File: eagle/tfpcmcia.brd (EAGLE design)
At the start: 80.4 x 44.4 mm, 36 parts, among them IC1 CH32V307, IC2 LM1117MPX-3.3, IC3 APS6404L-3SQR-SN, IC4 MCP6001RT-I_OT, J2 MSD-11-A

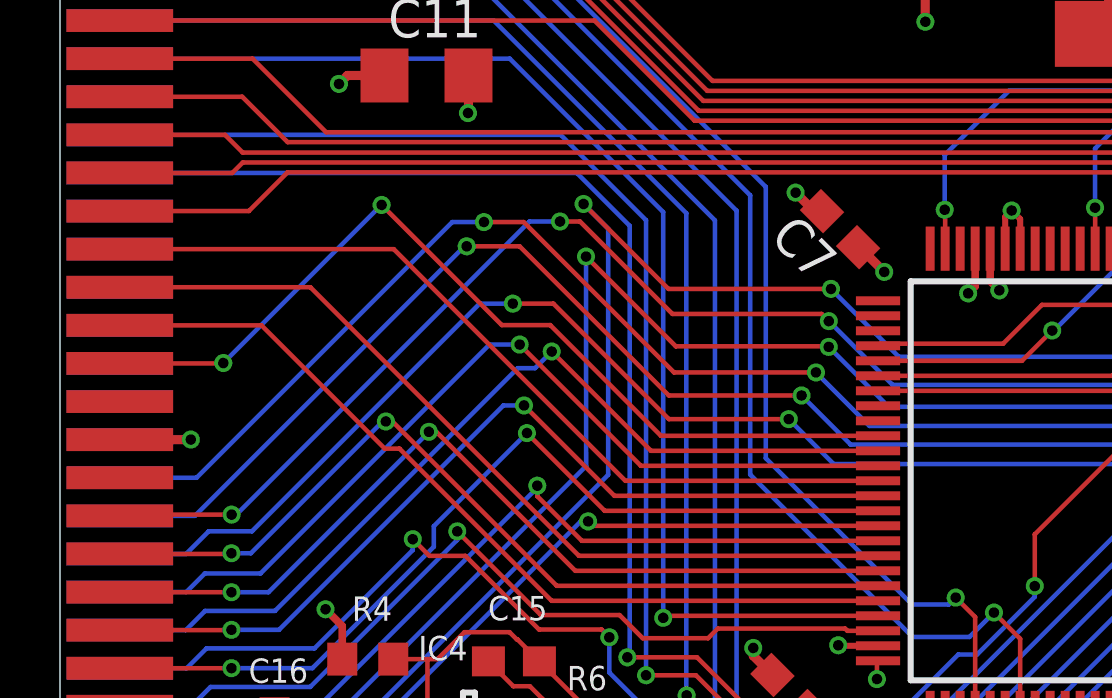
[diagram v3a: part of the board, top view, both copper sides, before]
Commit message: Updated READY signal and updated pinout specs
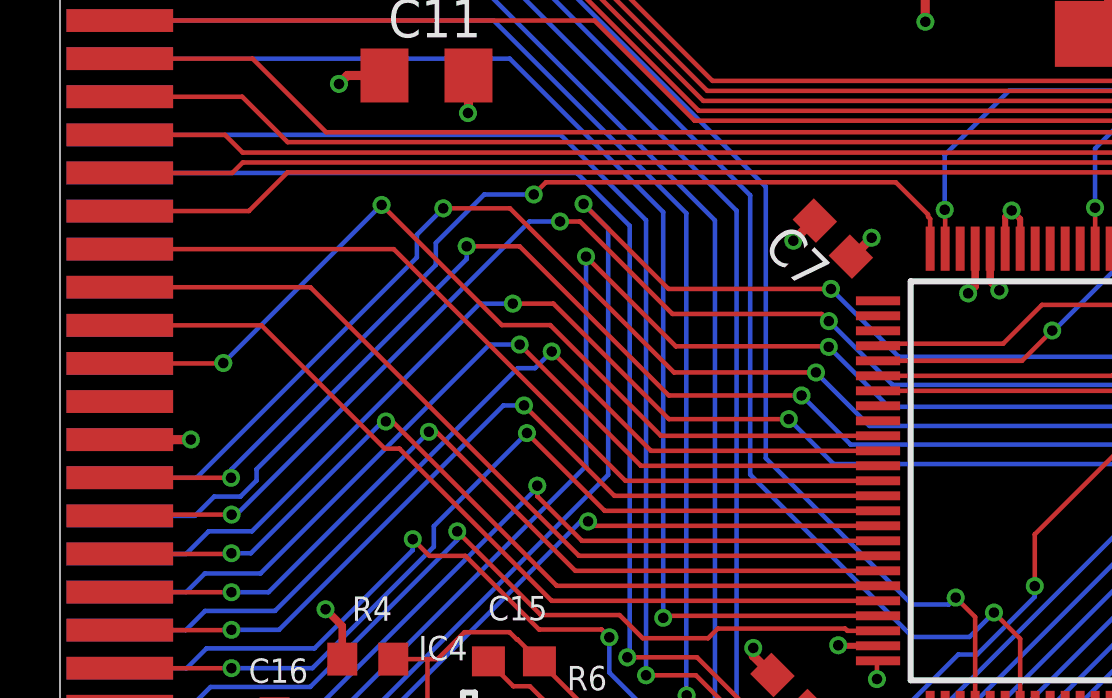
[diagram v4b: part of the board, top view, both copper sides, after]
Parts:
- moved C7 0.40 mm to (25.8, 28.2)
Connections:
- net READY: now also IC1.25
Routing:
- net READY: track 0.00 -> 33.2 mm, vias 0 -> 2
- net A21: track 47.2 -> 48.1 mm
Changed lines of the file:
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@@
 <attribute name="VALUE" x="42.162915625" y="28.52758125" size="1.27" layer="27" rot="R315"/>
 </element>
-<element name="C7" library="eagle-ltspice" library_urn="urn:adsk.eagle:library:217" package="C0603" package3d_urn="urn:adsk.eagle:package:13262/1" value="100nF" x="26.00196875" y="28.468321875" smashed="yes" rot="R135">
-<attribute name="NAME" x="26.00196875" y="27.57029375" size="1.27" layer="25" rot="R135"/>
-<attribute name="SPICEMODEL" value="NONE" x="26.00196875" y="28.468321875" size="0.8128" layer="27" rot="R135" display="off"/>
-<attribute name="SPICEPREFIX" value="C" x="26.00196875" y="28.468321875" size="0.8128" layer="27" rot="R135" display="off"/>
-<attribute name="VALUE" x="27.79801875" y="29.366346875" size="1.27" layer="27" rot="R135"/>
+<element name="C7" library="eagle-ltspice" library_urn="urn:adsk.eagle:library:217" package="C0603" package3d_urn="urn:adsk.eagle:package:13262/1" value="100nF" x="25.7622" y="28.153596875" smashed="yes" rot="R135">
+<attribute name="NAME" x="25.7622" y="27.25556875" size="1.27" layer="25" rot="R135"/>
+<attribute name="SPICEMODEL" value="NONE" x="25.7622" y="28.153596875" size="0.8128" layer="27" rot="R135" display="off"/>
+<attribute name="SPICEPREFIX" value="C" x="25.7622" y="28.153596875" size="0.8128" layer="27" rot="R135" display="off"/>
+<attribute name="VALUE" x="27.55825" y="29.051621875" size="1.27" layer="27" rot="R135"/>
 </element>
 <element name="C8" library="eagle-ltspice" library_urn="urn:adsk.eagle:library:217" package="C0603" package3d_urn="urn:adsk.eagle:package:13262/1" value="100nF" x="43.799840625" y="10.20089375" smashed="yes">
@@
 <contactref element="C9" pad="2"/>
 <via x="51.974821875" y="29.75490625" extent="1-16" drill="0.35"/>
-<via x="24.519659375" y="29.68626875" extent="1-16" drill="0.35"/>
+<via x="24.44473125" y="28.082671875" extent="1-16" drill="0.35"/>
 <via x="45.67343125" y="10.182284375" extent="1-16" drill="0.35"/>
 <via x="23.108325" y="14.508578125" extent="1-16" drill="0.35"/>
@@
 <wire x1="13.615446875" y1="32.354225" x2="13.599446875" y2="32.338225" width="0.3048" layer="1"/>
 <via x="13.599446875" y="32.338225" extent="1-16" drill="0.35"/>
-<wire x1="25.400925" y1="29.0693625" x2="25.136565625" y2="29.0693625" width="0.3048" layer="1"/>
-<wire x1="25.136565625" y1="29.0693625" x2="24.519659375" y2="29.68626875" width="0.3048" layer="1"/>
+<wire x1="25.16115625" y1="28.7546375" x2="25.116696875" y2="28.7546375" width="0.3048" layer="1"/>
+<wire x1="25.116696875" y1="28.7546375" x2="24.44473125" y2="28.082671875" width="0.3048" layer="1"/>
 <wire x1="48.549784375" y1="22.454765625" x2="48.61005625" y2="22.39449375" width="0.3048" layer="1"/>
 <wire x1="48.61005625" y1="22.39449375" x2="48.61005625" y2="21.304909375" width="0.3048" layer="1"/>
@@
 <signal name="READY">
 <contactref element="PCMCIA" pad="16"/>
+<wire x1="1.991615625" y1="20.18208125" x2="5.6981875" y2="20.18208125" width="0.1524" layer="1"/>
+<wire x1="5.6981875" y1="20.18208125" x2="5.701259375" y2="20.179009375" width="0.1524" layer="1"/>
+<via x="5.701259375" y="20.179009375" extent="1-16" drill="0.35"/>
+<wire x1="5.701259375" y1="20.179009375" x2="5.701259375" y2="20.44955" width="0.1524" layer="16"/>
+<wire x1="12.527703125" y1="27.27599375" x2="5.701259375" y2="20.44955" width="0.1524" layer="16"/>
+<wire x1="12.527703125" y1="27.27599375" x2="12.527703125" y2="28.010809375" width="0.1524" layer="16"/>
+<via x="15.79174375" y="29.624234375" extent="1-16" drill="0.35"/>
+<wire x1="15.79174375" y1="29.624234375" x2="16.198278125" y2="30.03076875" width="0.1524" layer="1"/>
+<contactref element="IC1" pad="25"/>
+<wire x1="28.9347875" y1="28.956984375" x2="28.9347875" y2="28.88495" width="0.1524" layer="1"/>
+<wire x1="28.9347875" y1="28.88495" x2="29.005509375" y2="28.814228125" width="0.1524" layer="1"/>
+<wire x1="29.005509375" y1="28.814228125" x2="29.005509375" y2="27.81800625" width="0.1524" layer="1"/>
+<wire x1="16.198278125" y1="30.03076875" x2="27.861003125" y2="30.03076875" width="0.1524" layer="1"/>
+<wire x1="27.861003125" y1="30.03076875" x2="28.9347875" y2="28.956984375" width="0.1524" layer="1"/>
+<wire x1="12.527703125" y1="28.010809375" x2="14.141128125" y2="29.624234375" width="0.1524" layer="16"/>
+<wire x1="14.141128125" y1="29.624234375" x2="15.79174375" y2="29.624234375" width="0.1524" layer="16"/>
 </signal>
 <signal name="VCC">
@@
 <contactref element="PCMCIA" pad="49"/>
 <contactref element="IC1" pad="90"/>
-<wire x1="13.48235" y1="27.897071875" x2="13.556803125" y2="27.897071875" width="0.1524" layer="16"/>
 <wire x1="42.743509375" y1="21.08000625" x2="37.259575" y2="21.08000625" width="0.1524" layer="1"/>
 <wire x1="37.259575" y1="21.08000625" x2="37.051959375" y2="21.287621875" width="0.1524" layer="1"/>
@@
 <wire x1="20.29363125" y1="22.9238875" x2="15.320446875" y2="27.897071875" width="0.1524" layer="1"/>
 <wire x1="1.991615625" y1="18.91208125" x2="4.497359375" y2="18.91208125" width="0.1524" layer="16"/>
-<wire x1="4.497359375" y1="18.91208125" x2="13.48235" y2="27.897071875" width="0.1524" layer="16"/>
+<wire x1="4.497359375" y1="18.91208125" x2="5.139271875" y2="19.55399375" width="0.1524" layer="16"/>
+<wire x1="13.556803125" y1="27.472684375" x2="13.556803125" y2="27.897071875" width="0.1524" layer="16"/>
+<wire x1="6.55244375" y1="20.468325" x2="13.556803125" y2="27.472684375" width="0.1524" layer="16"/>
+<wire x1="6.55244375" y1="20.09373125" x2="6.55244375" y2="20.468325" width="0.1524" layer="16"/>
+<wire x1="5.139271875" y1="19.55399375" x2="6.01270625" y2="19.55399375" width="0.1524" layer="16"/>
+<wire x1="6.01270625" y1="19.55399375" x2="6.55244375" y2="20.09373125" width="0.1524" layer="16"/>
 </signal>
 <signal name="A21">
@@
 <contactref element="IC1" pad="91"/>
 <wire x1="1.991615625" y1="20.18208125" x2="4.552246875" y2="20.18208125" width="0.1524" layer="16"/>
-<wire x1="13.075053125" y1="28.7048875" x2="4.552246875" y2="20.18208125" width="0.1524" layer="16"/>
-<wire x1="13.075053125" y1="28.7048875" x2="14.131571875" y2="28.7048875" width="0.1524" layer="16"/>
+<wire x1="11.8960125" y1="27.525846875" x2="4.552246875" y2="20.18208125" width="0.1524" layer="16"/>
 <wire x1="42.743509375" y1="21.58000625" x2="38.032721875" y2="21.58000625" width="0.1524" layer="1"/>
 <wire x1="38.032721875" y1="21.58000625" x2="37.7038625" y2="21.908865625" width="0.1524" layer="1"/>
@@
 <via x="25.19799375" y="23.692453125" extent="1-16" drill="0.35"/>
 <wire x1="25.19799375" y1="23.692453125" x2="20.468790625" y2="23.692453125" width="0.1524" layer="1"/>
-<wire x1="15.45635625" y1="28.7048875" x2="14.131571875" y2="28.7048875" width="0.1524" layer="1"/>
-<via x="14.131571875" y="28.7048875" extent="1-16" drill="0.35"/>
-<wire x1="20.468790625" y1="23.692453125" x2="15.45635625" y2="28.7048875" width="0.1524" layer="1"/>
+<wire x1="14.9992" y1="29.16204375" x2="12.775275" y2="29.16204375" width="0.1524" layer="1"/>
+<via x="12.775275" y="29.16204375" extent="1-16" drill="0.35"/>
+<wire x1="20.468790625" y1="23.692453125" x2="14.9992" y2="29.16204375" width="0.1524" layer="1"/>
+<wire x1="12.775275" y1="29.16204375" x2="11.8960125" y2="28.28278125" width="0.1524" layer="16"/>
+<wire x1="11.8960125" y1="28.28278125" x2="11.8960125" y2="27.525846875" width="0.1524" layer="16"/>
 </signal>
 <signal name="A22">
@@
 <contactref element="C9" pad="1"/>
 <via x="52.0015875" y="33.392221875" extent="1-16" drill="0.35"/>
-<via x="27.47450625" y="27.043275" extent="1-16" drill="0.35"/>
+<via x="27.0549125" y="28.182278125" extent="1-16" drill="0.35"/>
 <wire x1="41.880825" y1="10.20089375" x2="41.8673125" y2="10.21440625" width="0.1524" layer="1"/>
 <via x="41.8673125" y="10.21440625" extent="1-16" drill="0.35"/>
@@
 <via x="42.61121875" y="30.702096875" extent="1-16" drill="0.35"/>
 <via x="45.696228125" y="22.461528125" extent="1-16" drill="0.35"/>
-<wire x1="26.603009375" y1="27.867278125" x2="26.650503125" y2="27.867278125" width="0.3048" layer="1"/>
-<wire x1="26.650503125" y1="27.867278125" x2="27.47450625" y2="27.043275" width="0.3048" layer="1"/>
+<wire x1="26.363240625" y1="27.552553125" x2="26.4251875" y2="27.552553125" width="0.3048" layer="1"/>
+<wire x1="26.4251875" y1="27.552553125" x2="27.0549125" y2="28.182278125" width="0.3048" layer="1"/>
 <wire x1="45.696228125" y1="22.461528125" x2="46.843021875" y2="22.461528125" width="0.3048" layer="1"/>
 <wire x1="46.843021875" y1="22.461528125" x2="46.849784375" y2="22.454765625" width="0.3048" layer="1"/>

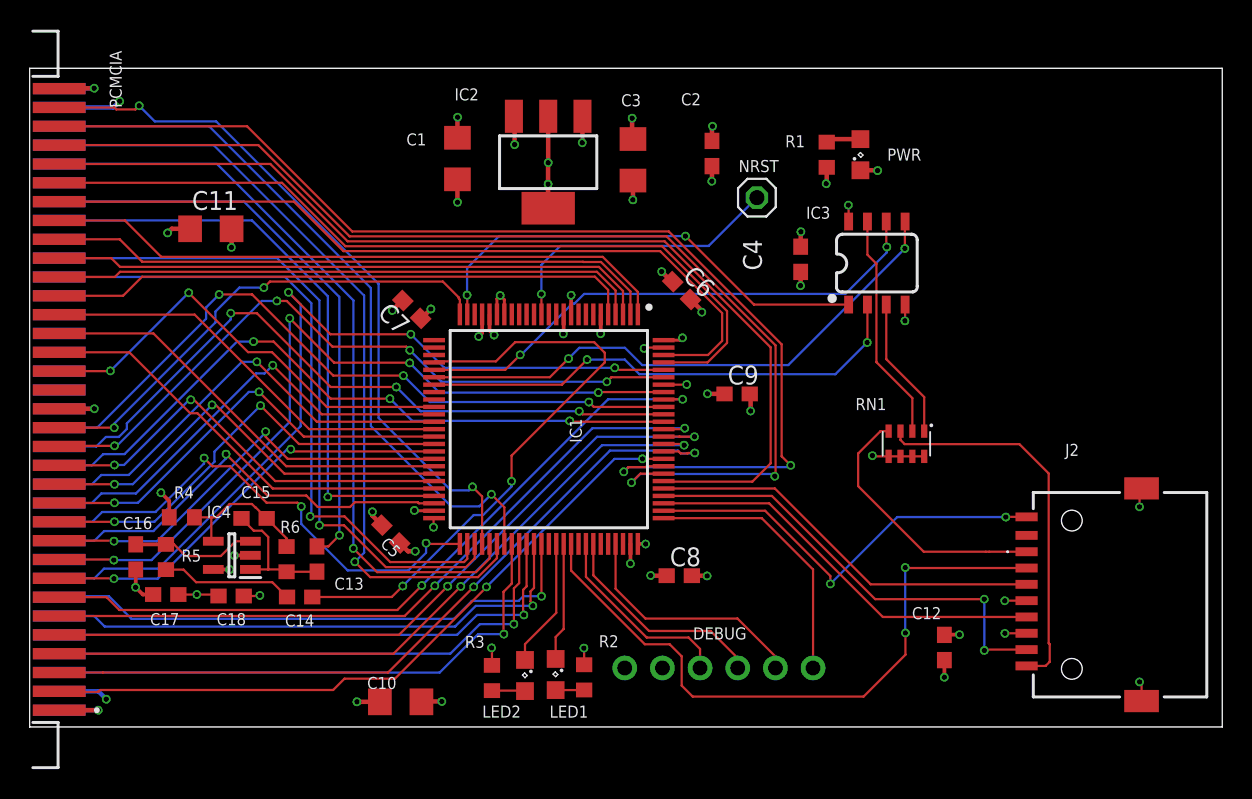
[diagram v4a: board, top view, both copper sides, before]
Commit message: added blinkenlights and gathered notes on spi ram usage
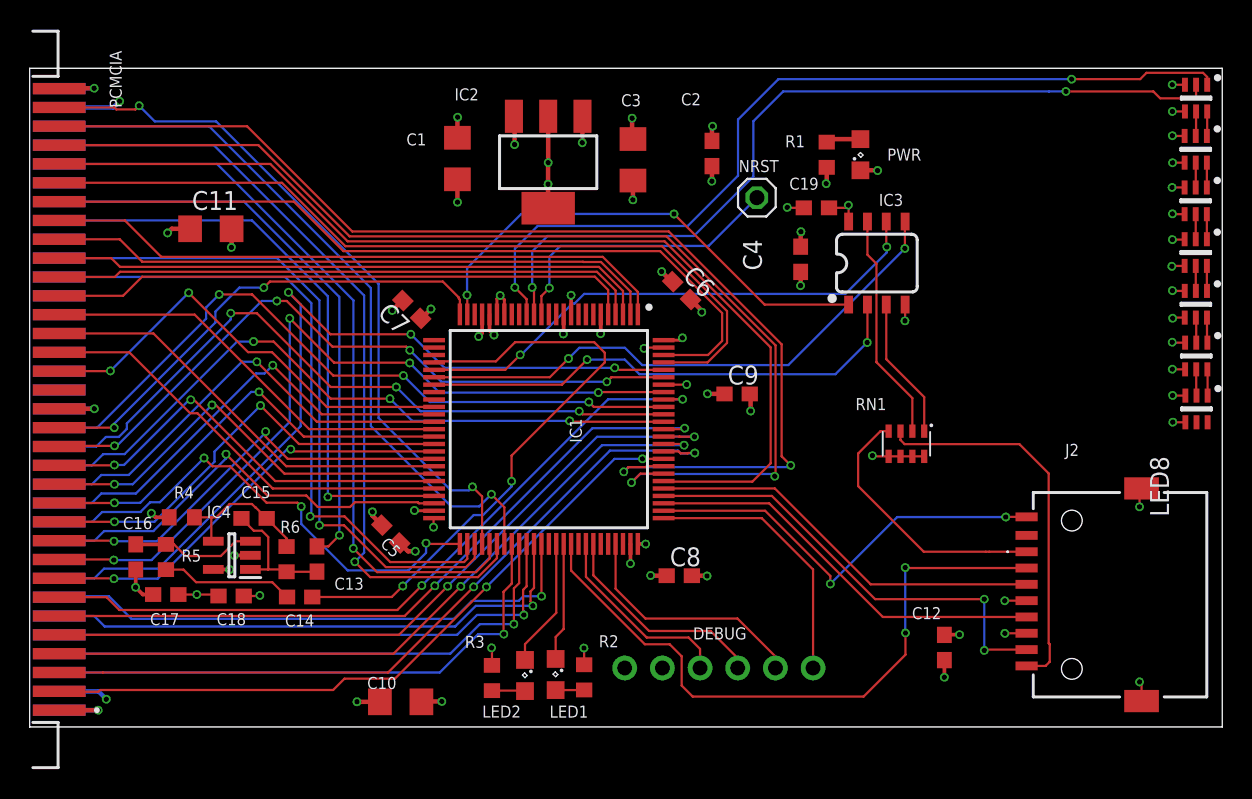
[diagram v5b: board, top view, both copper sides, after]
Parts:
- added C19: 1uF, eagle-ltspice:C0603
- added LED3, LED4, LED5, LED6, LED7, LED8, LED9: COM-14608, Blinkenlights:SON75P200X200X100-6N
- IC3: value APS6404L-3SQR-SN -> 32M SPI Flash
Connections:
- new net LED_CLK: IC1.15, LED3.2
- new net LED_DO: IC1.16, LED3.1
- new net N$11: LED4.5, LED5.2
- new net N$12: LED4.6, LED5.1
- new net N$13: LED5.6, LED6.1
- new net N$14: LED5.5, LED6.2
- new net N$15: LED3.5, LED4.2
- new net N$16: LED3.6, LED4.1
- new net N$17: LED6.5, LED7.2
- new net N$19: LED6.6, LED7.1
- new net N$20: LED7.6, LED8.1
- new net N$21: LED7.5, LED8.2
- new net N$22: LED8.5, LED9.2
- new net N$23: LED8.6, LED9.1
- net GND: now also C19.2, LED3.3, LED4.3, LED5.3, LED6.3, LED7.3, LED8.3, LED9.3
- net VCC: now also LED3.4, LED4.4, LED5.4, LED6.4, LED7.4, LED8.4, LED9.4
- net VCC33: now also C19.1
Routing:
- net LED_DO: track 0.00 -> 59.2 mm, vias 0 -> 2
- net LED_CLK: track 0.00 -> 56.7 mm, vias 0 -> 2
- net GND: track 56.4 -> 62.9 mm, vias 32 -> 40
- net VCC: track 16.1 -> 22.0 mm, vias 8 -> 15
- net N$23: track 0.00 -> 1.78 mm
- net N$22: track 0.00 -> 1.78 mm
- net N$21: track 0.00 -> 1.70 mm
- net N$20: track 0.00 -> 1.70 mm
- net N$19: track 0.00 -> 1.69 mm
- net N$17: track 0.00 -> 1.69 mm
- net N$14: track 0.00 -> 1.69 mm
- net N$13: track 0.00 -> 1.69 mm
- net N$12: track 0.00 -> 1.68 mm
- net N$11: track 0.00 -> 1.68 mm
- net N$16: track 0.00 -> 1.66 mm
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
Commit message: tightened DRC
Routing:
- net D5: track 49.4 -> 50.1 mm
- net GND: track 62.9 -> 63.4 mm
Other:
- board text added: "(C) 2026 - S.J. Leary, A. Makarenko & E. Hemming"

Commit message: add initial firmware: CH32V307 PCMCIA bus emulation returning BEEF/BABE
- Dockerised build using local MRS toolchain (riscv-none-embed-gcc)
- EXTI9_5 VTF interrupt handler drives data bus on UDS/LDS assertion
- Common memory returns 0xBEEF, attribute memory returns 0xBABE
- BUS16() macro compensates for Gayle byte-lane swap on A600/A1200
- UART debug on PA9 at 115200, heartbeat LED on PC8
- Top-level Makefile delegates build/clean to Docker container
- DiagROM helper scripts in scripts/
- Updated .gitignore for firmware build artefacts and MRS installer
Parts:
- IC3: value 32M SPI Flash -> APS6404L
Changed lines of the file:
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@@
 <attribute name="VALUE" x="56.464421875" y="20.83614375" size="0.8128" layer="27" rot="R270" align="center"/>
 </element>
-<element name="IC3" library="SparkFun-IC-Memory" package="SO08" value="32M SPI Flash" x="57.121509375" y="31.279446875" smashed="yes">
+<element name="IC3" library="SparkFun-IC-Memory" package="SO08" value="APS6404L" x="57.121509375" y="31.279446875" smashed="yes">
 <attribute name="NAME" x="58.076653125" y="35.535075" size="0.8128" layer="25" font="fixed" ratio="20" rot="R180" align="center"/>
 <attribute name="PROD_ID" value="N/A" x="57.121509375" y="31.279446875" size="1.778" layer="27" display="off"/>

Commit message: Board updates for revision 1
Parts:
- added JP1, JP2: (no value), SparkFun-Retired:1X02
- added R7: 2K2, rcl:R0603
- R1: value 10k -> 2K2
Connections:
- new net BOOT0: IC1.94, JP2.1, R7.2
- new net USB1_DM: IC1.70, JP1.2
- new net USB1_DP: IC1.71, JP1.1
- net GND: now also R7.1; no longer IC1.94
- net RAM_MISO: now also IC1.31; no longer IC1.32
- net RAM_MOSI: now also IC1.32; no longer IC1.31
- net VCC33: now also JP2.2
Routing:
- net BOOT0: track 0.00 -> 16.1 mm, vias 0 -> 1
- net USB1_DM: track 0.00 -> 13.5 mm
- net USB1_DP: track 0.00 -> 12.8 mm
- net SWDIO: track 16.5 -> 21.7 mm
- net GND: track 63.4 -> 62.7 mm
